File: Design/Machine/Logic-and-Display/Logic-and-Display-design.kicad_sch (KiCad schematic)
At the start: 1 part, among them J1 Jack-DC-5V

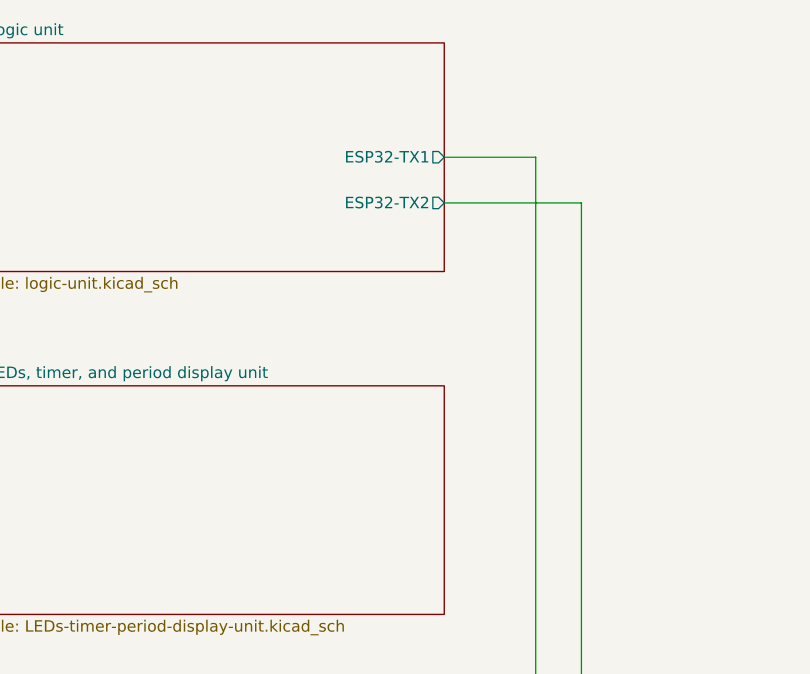
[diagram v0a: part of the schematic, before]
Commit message: feat: schematics w/out buzzer, some LEDS, matrix
add schematics for LEDs and time display, missing FC-16 module (8x32 matrix) connection, left priority, right side LEDS, and buzzer
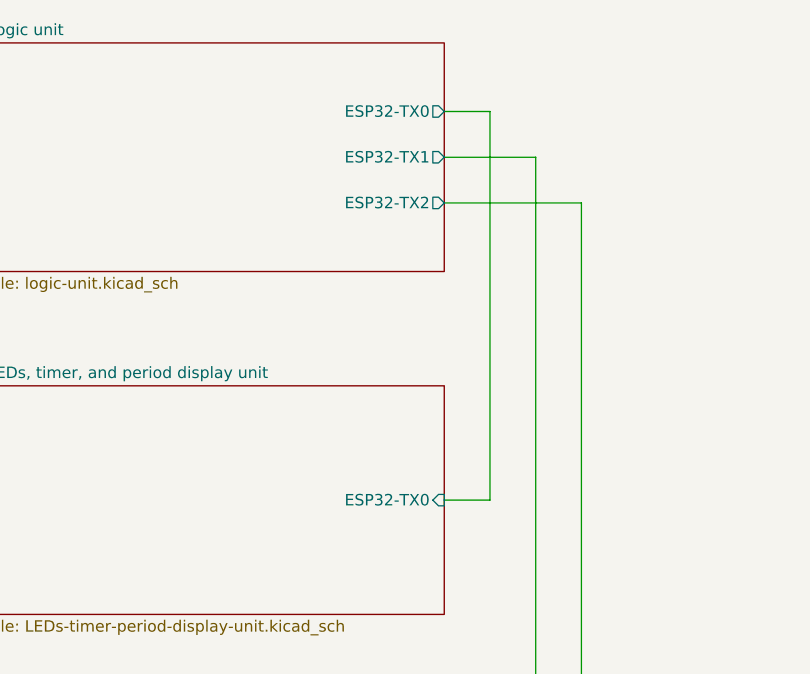
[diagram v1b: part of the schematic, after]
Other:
- sheet LEDs, timer, and period display unit ports: added ESP32-TX0; removed none
- sheet Logic unit ports: added ESP32-TX0; removed none
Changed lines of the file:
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@@
+    (stroke (width 0) (type default))
+  )
+  (wire (pts (xy 132.08 33.02) (xy 132.08 76.2))
+    (stroke (width 0) (type default))
+  )
+  (wire (pts (xy 127 33.02) (xy 132.08 33.02))
     (stroke (width 0) (type default))
   )
@@
     (stroke (width 0) (type default))
   )
+  (wire (pts (xy 132.08 76.2) (xy 127 76.2))
+    (stroke (width 0) (type default))
+  )
   (symbol (lib_id "power:PWR_FLAG") (at 198.12 77.47 0) (unit 1)
     (in_bom yes) (on_board yes) (dnp no) (fields_autoplaced)
@@
   (symbol (lib_id "power:GND") (at 208.28 82.55 0) (unit 1)
     (in_bom yes) (on_board yes) (dnp no) (fields_autoplaced)
-    (property "Reference" "#PWR01" (at 208.28 88.9 0)
+    (property "Reference" "#PWR02" (at 208.28 88.9 0)
       (effects (font (size 1.27 1.27)) hide)
     )
@@
   (symbol (lib_id "power:+5V") (at 208.28 77.47 0) (unit 1)
     (in_bom yes) (on_board yes) (dnp no) (fields_autoplaced)
-    (property "Reference" "#PWR02" (at 208.28 81.28 0)
+    (property "Reference" "#PWR01" (at 208.28 81.28 0)
       (effects (font (size 1.27 1.27)) hide)
     )
@@
       (effects (font (size 1.27 1.27)) (justify left top))
     )
+    (pin "ESP32-TX0" input (at 127 76.2 0)
+      (effects (font (size 1.27 1.27)) (justify right))
+    )
     (instances
       (project "Logic-and-Display-design"
@@
       (effects (font (size 1.27 1.27)) (justify right))
     )
+    (pin "ESP32-TX0" output (at 127 33.02 0)
+      (effects (font (size 1.27 1.27)) (justify right))
+    )

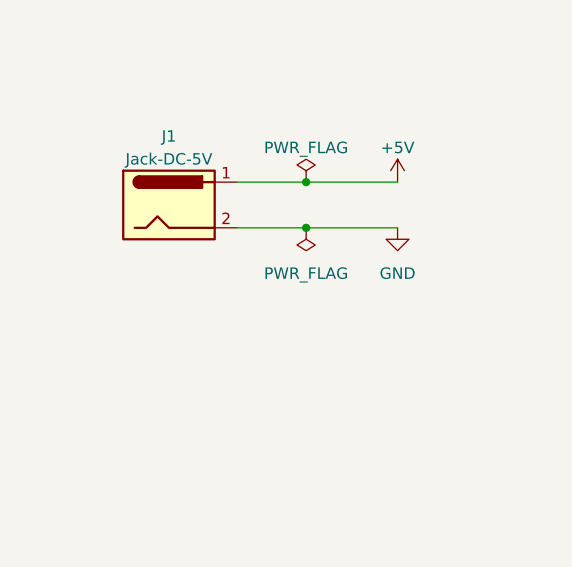
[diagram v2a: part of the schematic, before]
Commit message: feat: logic and display units schecmatics
complete logic and display units schematics
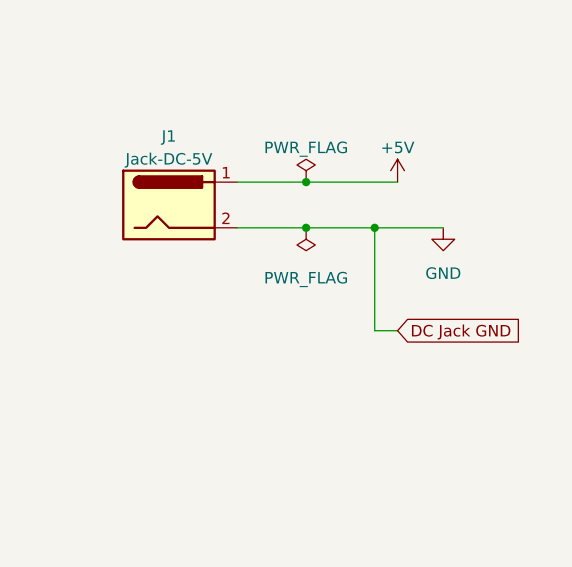
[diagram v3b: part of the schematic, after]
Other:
- title: Logic and display units schematis -> Logic and display units schematics
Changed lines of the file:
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@@
   (paper "A4")
   (title_block
-    (title "Logic and display units schematis")
-    (date "2023-05-19")
-    (rev "0.1.0")
+    (title "Logic and display units schematics")
+    (date "2023-06-14")
+    (rev "1.0.0")
     (comment 1 "Pending logic unit schematics")
   )
-  (junction (at 198.12 82.55) (diameter 0) (color 0 0 0 0)
+  (junction (at 205.74 82.55) (diameter 0) (color 0 0 0 0)
   )
   (junction (at 198.12 77.47) (diameter 0) (color 0 0 0 0)
+  )
+  (junction (at 198.12 82.55) (diameter 0) (color 0 0 0 0)
   )
   (wire (pts (xy 190.5 82.55) (xy 198.12 82.55))
@@
     (stroke (width 0) (type default))
   )
+  (wire (pts (xy 205.74 82.55) (xy 213.36 82.55))
+    (stroke (width 0) (type default))
+  )
   (wire (pts (xy 190.5 77.47) (xy 198.12 77.47))
+    (stroke (width 0) (type default))
+  )
+  (wire (pts (xy 205.74 93.98) (xy 205.74 82.55))
     (stroke (width 0) (type default))
   )
@@
     (stroke (width 0) (type default))
   )
-  (wire (pts (xy 198.12 82.55) (xy 208.28 82.55))
+  (wire (pts (xy 127 38.1) (xy 137.16 38.1))
     (stroke (width 0) (type default))
   )
-  (wire (pts (xy 127 38.1) (xy 137.16 38.1))
+  (wire (pts (xy 198.12 82.55) (xy 205.74 82.55))
     (stroke (width 0) (type default))
   )
@@
   (wire (pts (xy 132.08 76.2) (xy 127 76.2))
     (stroke (width 0) (type default))
+  )
+  (wire (pts (xy 208.28 93.98) (xy 205.74 93.98))
+    (stroke (width 0) (type default))
+  )
+  (global_label "DC Jack GND" (shape input) (at 208.28 93.98 0) (fields_autoplaced)
+    (effects (font (size 1.27 1.27)) (justify left))
+    (property "Intersheetrefs" "${INTERSHEET_REFS}" (at 223.7648 93.98 0)
+      (effects (font (size 1.27 1.27)) (justify left) hide)
+    )
   )
   (symbol (lib_id "power:PWR_FLAG") (at 198.12 77.47 0) (unit 1)
@@
         (path "/4a7d315f-bdf1-40ee-ab6c-d5952306d95d"
           (reference "#FLG01") (unit 1)
+        )
+      )
+    )
+  )
+  (symbol (lib_id "power:PWR_FLAG") (at 198.12 82.55 180) (unit 1)
+    (in_bom yes) (on_board yes) (dnp no) (fields_autoplaced)
+    (property "Reference" "#FLG02" (at 198.12 84.455 0)
+      (effects (font (size 1.27 1.27)) hide)
+    )
+    (property "Value" "PWR_FLAG" (at 198.12 88.138 0)
+      (effects (font (size 1.27 1.27)))
+    )
+    (property "Footprint" "" (at 198.12 82.55 0)
+      (effects (font (size 1.27 1.27)) hide)
+    )
+    (property "Datasheet" "~" (at 198.12 82.55 0)
+      (effects (font (size 1.27 1.27)) hide)
+    )
+    (pin "1")
+    (instances
+      (project "Logic-and-Display-design"
+        (path "/4a7d315f-bdf1-40ee-ab6c-d5952306d95d"
+          (reference "#FLG02") (unit 1)
         )
       )
@@
     )
   )
-  (symbol (lib_id "power:GND") (at 208.28 82.55 0) (unit 1)
+  (symbol (lib_id "power:GND") (at 213.36 82.55 0) (unit 1)
     (in_bom yes) (on_board yes) (dnp no) (fields_autoplaced)
-    (property "Reference" "#PWR02" (at 208.28 88.9 0)
+    (property "Reference" "#PWR02" (at 213.36 88.9 0)
       (effects (font (size 1.27 1.27)) hide)
     )
-    (property "Value" "GND" (at 208.28 87.63 0)
+    (property "Value" "GND" (at 213.36 87.63 0)
       (effects (font (size 1.27 1.27)))
     )
-    (property "Footprint" "" (at 208.28 82.55 0)
+    (property "Footprint" "" (at 213.36 82.55 0)
       (effects (font (size 1.27 1.27)) hide)
     )
-    (property "Datasheet" "" (at 208.28 82.55 0)
+    (property "Datasheet" "" (at 213.36 82.55 0)
       (effects (font (size 1.27 1.27)) hide)
     )
@@
         )
       )
-    )
-  )
-  (symbol (lib_id "power:PWR_FLAG") (at 198.12 82.55 180) (unit 1)
-    (in_bom yes) (on_board yes) (dnp no) (fields_autoplaced)
-    (property "Reference" "#FLG02" (at 198.12 84.455 0)
-      (effects (font (size 1.27 1.27)) hide)
-    )
-    (property "Value" "PWR_FLAG" (at 198.12 87.63 0)
-      (effects (font (size 1.27 1.27)))
-    )
-    (property "Footprint" "" (at 198.12 82.55 0)
-      (effects (font (size 1.27 1.27)) hide)
-    )
-    (property "Datasheet" "~" (at 198.12 82.55 0)
-      (effects (font (size 1.27 1.27)) hide)
-    )
-    (pin "1")
-    (instances
-      (project "Logic-and-Display-design"
-        (path "/4a7d315f-bdf1-40ee-ab6c-d5952306d95d"
-          (reference "#FLG02") (unit 1)
-        )
-      )

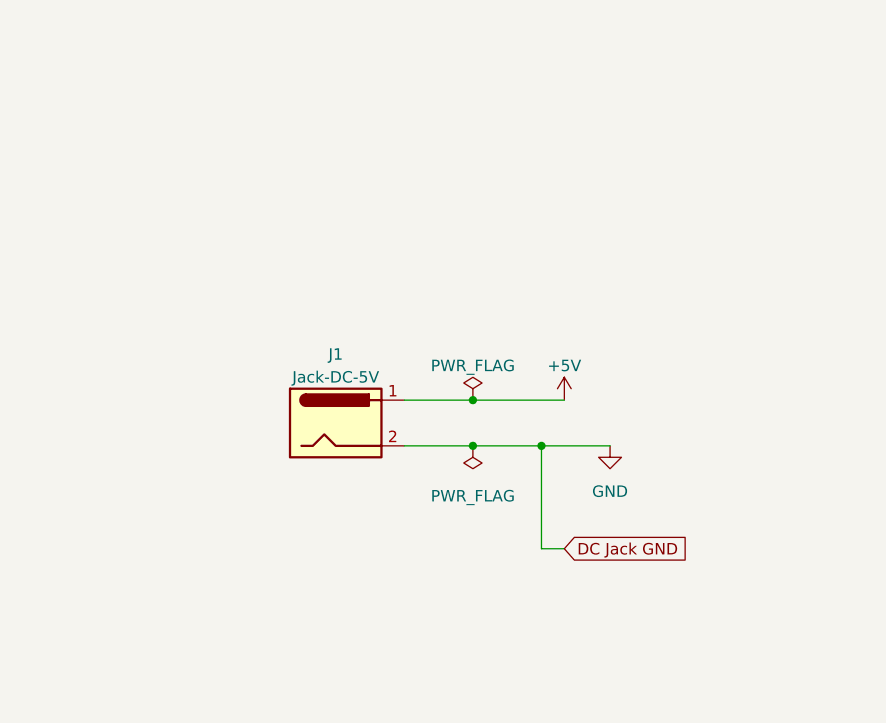
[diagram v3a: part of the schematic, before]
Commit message: fix: logic and display units on/off switch
include a DPST switch to disconnect battery and DC jack
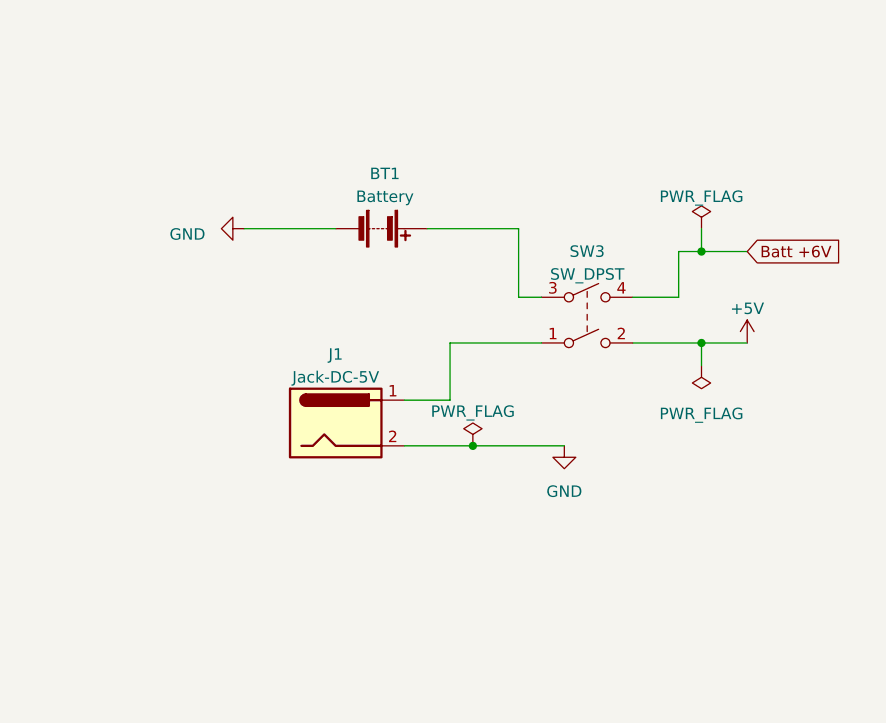
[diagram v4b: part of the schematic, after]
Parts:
- added BT1: Battery, Connector_PinSocket_2.54mm:PinSocket_1x02_P2.54mm_Vertical, symbol Device:Battery
- added SW3: SW_DPST, symbol Switch:SW_DPST
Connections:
- net +5V: now also SW3.2; no longer J1.1
- net GND: now also BT1.2 (-)
- new net: J1.1, SW3.1
- new net: BT1.1 (+), SW3.3
- new net Batt +6V: SW3.4

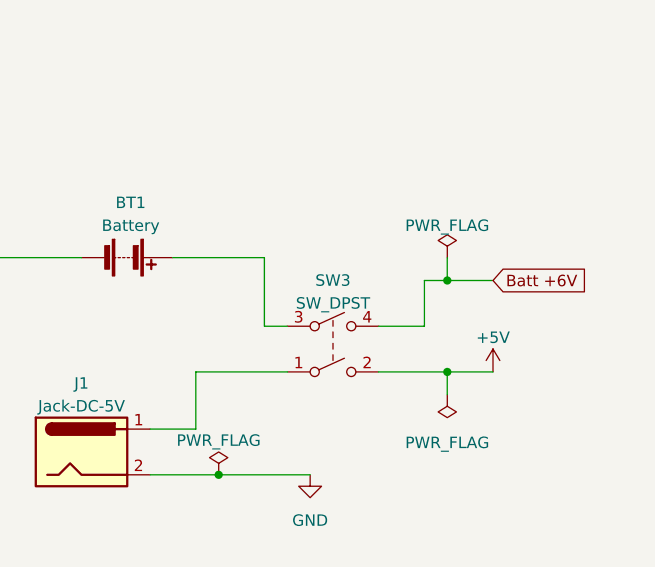
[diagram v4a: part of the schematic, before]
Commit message: feat: double pole triple throw switch
make on/off switch a double pole triple throw switch (DP3T), previously DPDT so that there is an option to turn on with redundancy
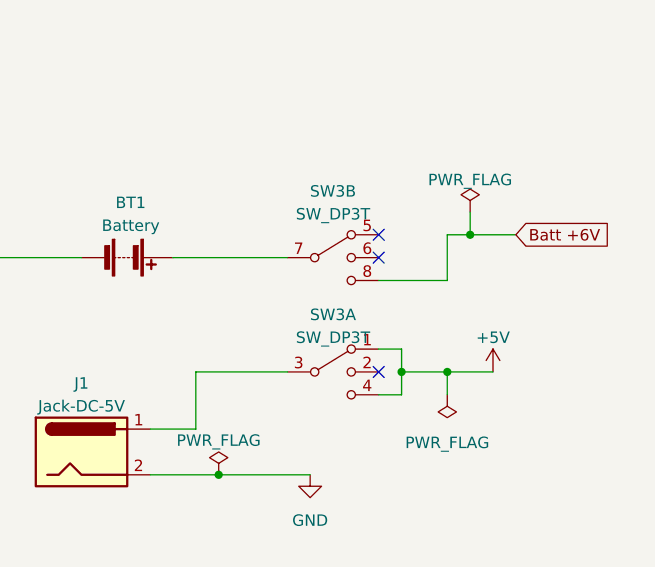
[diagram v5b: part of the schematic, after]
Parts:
- removed SW3: SW_DPST, symbol Switch:SW_DPST
- added SW3: SW_DP3T, symbol Switch:SW_DP3T
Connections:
- net +5V: now also SW3.1, SW3.4
- net Batt +6V: now also SW3.8
- net at J1.1: now also SW3.3
- net at BT1.1 (+): now also SW3.7
- no-connect marks 0 -> 3
